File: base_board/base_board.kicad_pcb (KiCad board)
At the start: 2 copper layers, 18 parts, among them J1 Conn_ARM_JTAG_SWD_20, U1 STM32F446ZEJx, U2 IS42S16400J-xT, U3 BMI270

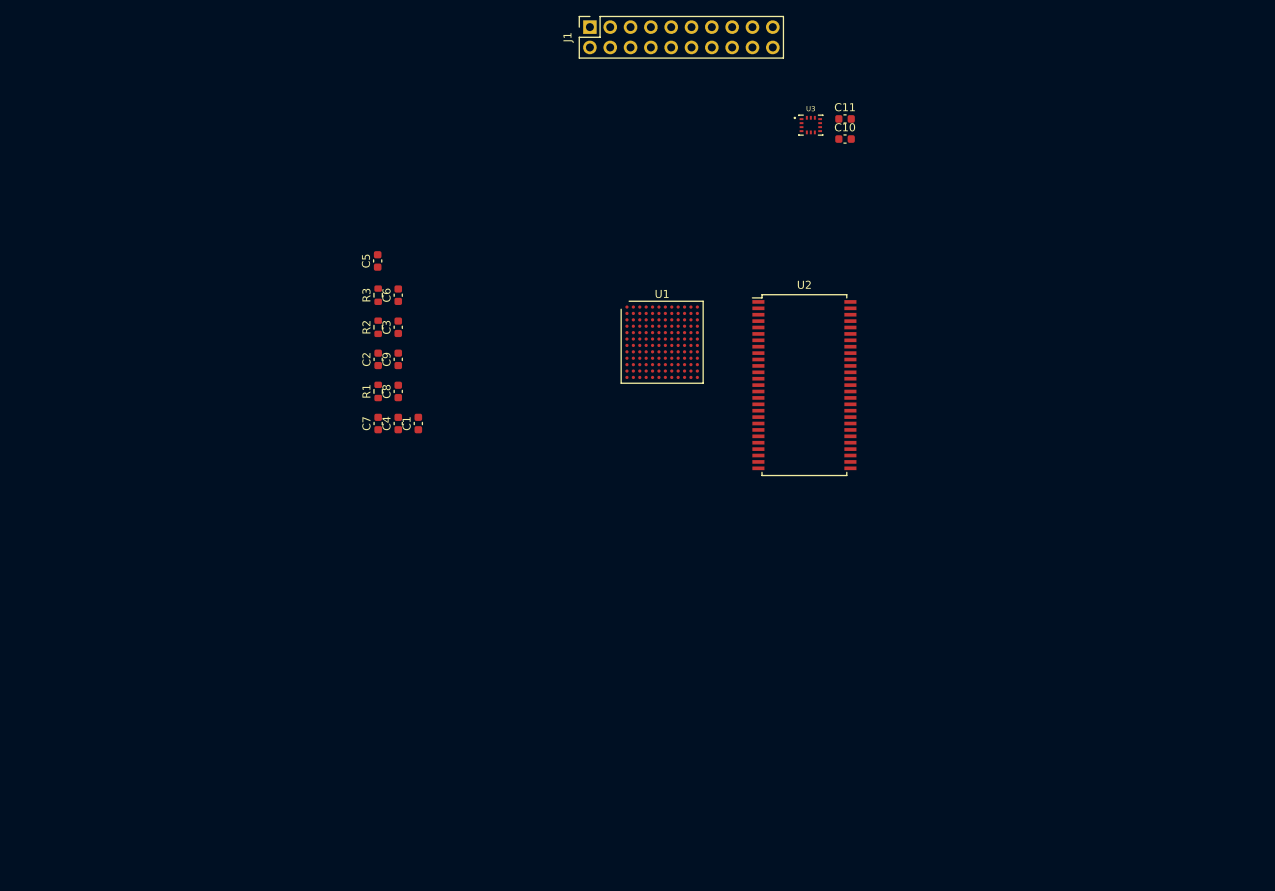
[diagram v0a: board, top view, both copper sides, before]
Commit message: [pcb][cube][schematic] added SWD, Crystal, USB
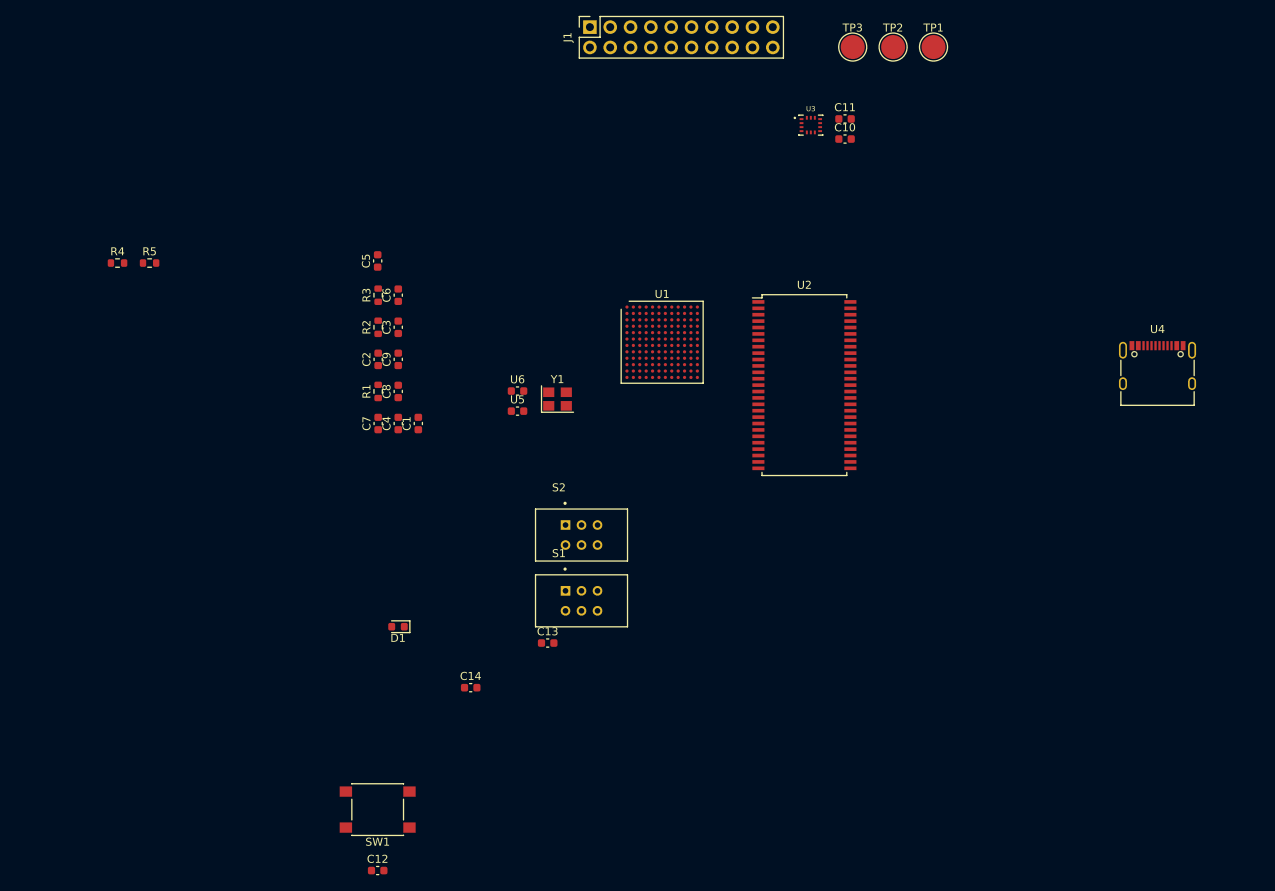
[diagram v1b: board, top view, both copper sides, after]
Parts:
- added C12: 100nF, Capacitor_SMD:C_0603_1608Metric, F.Cu at (96.5, 154.9)
- added C13: 2.2uF, Capacitor_SMD:C_0603_1608Metric, F.Cu at (117.8, 126.5)
- added C14: 2.2uF, Capacitor_SMD:C_0603_1608Metric, F.Cu at (108.2, 132.1)
- added D1: LED, LED_SMD:LED_0603_1608Metric, F.Cu at (99.1, 124.5)
- added R4: 5.1k, Resistor_SMD:R_0603_1608Metric, F.Cu at (64.0, 79.0)
- added R5: 5.1k, Resistor_SMD:R_0603_1608Metric, F.Cu at (68.0, 79.0)
- added S1: EG2209A, project_switch:SW_EG2209A, F.Cu at (122.0, 121.2)
- added S2: EG2209A, project_switch:SW_EG2209A, F.Cu at (122.0, 113.0)
- added SW1: SW_Push, Button_Switch_SMD:SW_Push_1P1T_NO_6x6mm_H9.5mm, F.Cu at (96.5, 147.3)
- added TP1: TestPoint, TestPoint:TestPoint_Pad_D3.0mm, F.Cu at (166.0, 52.0)
- added TP2: TestPoint, TestPoint:TestPoint_Pad_D3.0mm, F.Cu at (160.9, 52.0)
- added TP3: TestPoint, TestPoint:TestPoint_Pad_D3.0mm, F.Cu at (155.9, 52.0)
- added U4: USB_C_Receptacle_USB2.0, project_typec:USB_C_Receptacle_XKB_U262-16XN-4BVC11, F.Cu at (194.0, 93.0)
- added U5: 10p, Capacitor_SMD:C_0603_1608Metric, F.Cu at (114.0, 97.5)
- added U6: 10p, Capacitor_SMD:C_0603_1608Metric, F.Cu at (114.0, 95.0)
- added Y1: Crystal_GND24, Crystal:Crystal_SMD_3225-4Pin_3.2x2.5mm, F.Cu at (119.0, 96.0)
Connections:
- U1 pad C11: unconnected-(U1-PadC11) -> +3.3V
- U1 pad D1: unconnected-(U1-PadD1) -> /HSE_IN
- U1 pad D2: unconnected-(U1-PadD2) -> GND
- U1 pad D3: unconnected-(U1-PadD3) -> +3.3V
- U1 pad E1: unconnected-(U1-PadE1) -> /HSE_OUT
- U1 pad E6: unconnected-(U1-PadE6) -> GND
- U1 pad E7: unconnected-(U1-PadE7) -> GND
- U1 pad F1: unconnected-(U1-PadF1) -> /RESET
- U1 pad F10: unconnected-(U1-PadF10) -> +3.3V
- U1 pad F4: unconnected-(U1-PadF4) -> +3.3V
- U1 pad F5: unconnected-(U1-PadF5) -> +3.3V
- U1 pad F6: unconnected-(U1-PadF6) -> +3.3V
- U1 pad F7: unconnected-(U1-PadF7) -> +3.3V
- U1 pad F8: unconnected-(U1-PadF8) -> +3.3V
- U1 pad F9: unconnected-(U1-PadF9) -> +3.3V
- U1 pad G10: unconnected-(U1-PadG10) -> GND
- U1 pad G4: unconnected-(U1-PadG4) -> GND
- U1 pad G5: unconnected-(U1-PadG5) -> +3.3V
- U1 pad G6: unconnected-(U1-PadG6) -> +3.3V
- U1 pad G7: unconnected-(U1-PadG7) -> +3.3V
- U1 pad G8: unconnected-(U1-PadG8) -> GND
- U1 pad G9: unconnected-(U1-PadG9) -> Net-(C14-Pad2)
- U1 pad H6: unconnected-(U1-PadH6) -> GND
- U1 pad H7: unconnected-(U1-PadH7) -> Net-(C13-Pad2)
- U1 pad J1: unconnected-(U1-PadJ1) -> GND
- U1 pad M1: unconnected-(U1-PadM1) -> +3.3V
- U3 pad 1: unconnected-(U3-Pad1) -> Net-(TP1-Pad1)
- U3 pad 13: unconnected-(U3-Pad13) -> Net-(TP3-Pad1)
- U3 pad 14: unconnected-(U3-Pad14) -> Net-(TP2-Pad1)

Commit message: [schematic][pcb] added usb, signal leds, LDO
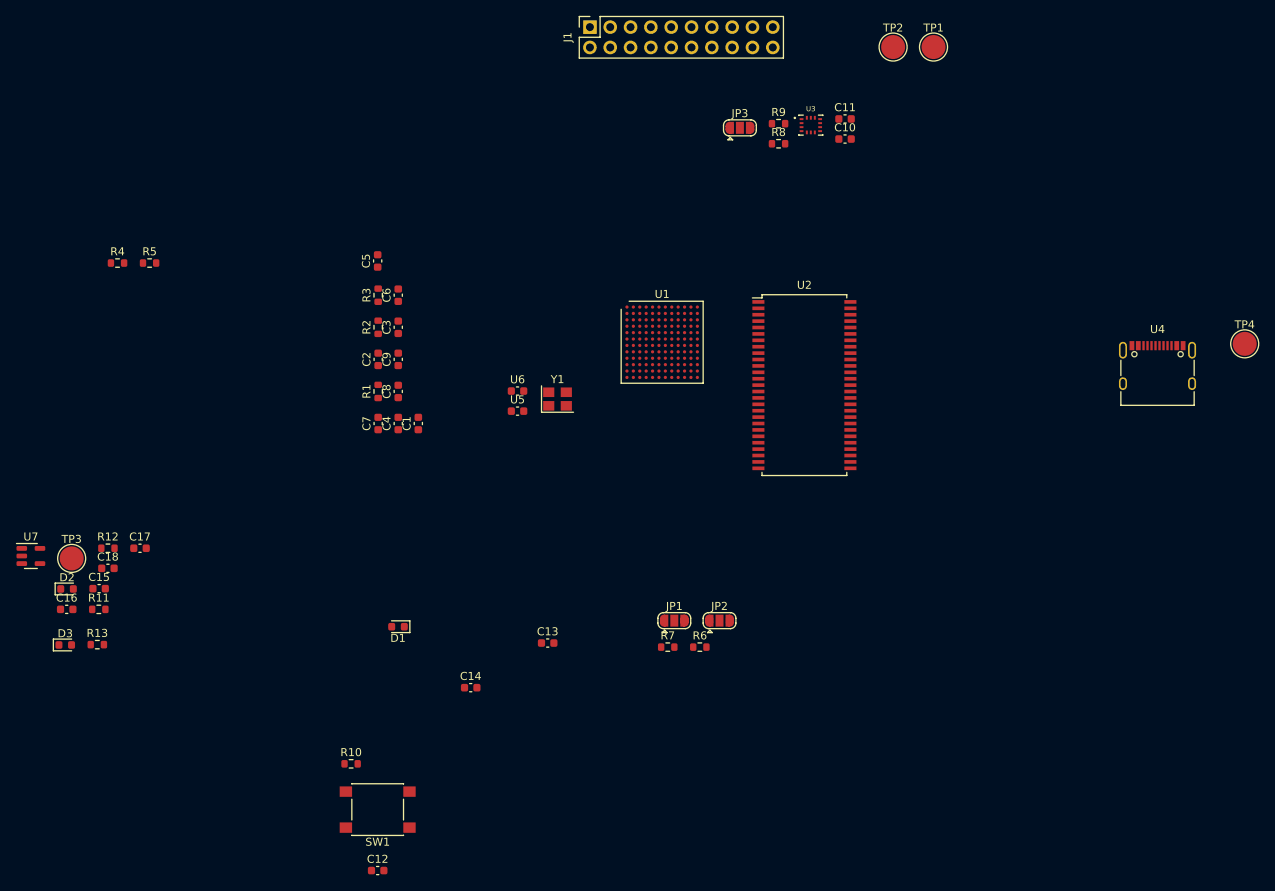
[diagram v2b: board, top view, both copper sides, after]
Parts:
- removed S1, S2: EG2209A, project_switch:SW_EG2209A
- added C15: 1uF, Capacitor_SMD:C_0603_1608Metric, F.Cu at (61.7, 119.7)
- added C16: 100nF, Capacitor_SMD:C_0603_1608Metric, F.Cu at (57.6, 122.3)
- added C17: 10nF, Capacitor_SMD:C_0603_1608Metric, F.Cu at (66.8, 114.7)
- added C18: 1uF, Capacitor_SMD:C_0603_1608Metric, F.Cu at (62.8, 117.2)
- added D2: LED, LED_SMD:LED_0603_1608Metric, F.Cu at (57.7, 119.7)
- added D3: LED, LED_SMD:LED_0603_1608Metric, F.Cu at (57.5, 126.7)
- added JP1: SolderJumper_3_Open, Jumper:SolderJumper-3_P1.3mm_Open_RoundedPad1.0x1.5mm, F.Cu at (133.6, 123.7)
- added JP2: SolderJumper_3_Open, Jumper:SolderJumper-3_P1.3mm_Open_RoundedPad1.0x1.5mm, F.Cu at (139.2, 123.7)
- added JP3: SolderJumper_3_Open, Jumper:SolderJumper-3_P1.3mm_Open_RoundedPad1.0x1.5mm, F.Cu at (141.8, 62.1)
- added R10: 10K, Resistor_SMD:R_0603_1608Metric, F.Cu at (93.2, 141.6)
- added R11: 510, Resistor_SMD:R_0603_1608Metric, F.Cu at (61.7, 122.3)
- added R12: 510, Resistor_SMD:R_0603_1608Metric, F.Cu at (62.8, 114.7)
- added R13: 510, Resistor_SMD:R_0603_1608Metric, F.Cu at (61.5, 126.7)
- added R6: 10K, Resistor_SMD:R_0603_1608Metric, F.Cu at (136.8, 127.0)
- added R7: 10K, Resistor_SMD:R_0603_1608Metric, F.Cu at (132.8, 127.0)
- added R8: 4.7K, Resistor_SMD:R_0603_1608Metric, F.Cu at (146.6, 64.1)
- added R9: 4.7K, Resistor_SMD:R_0603_1608Metric, F.Cu at (146.6, 61.6)
- added TP4: TestPoint, TestPoint:TestPoint_Pad_D3.0mm, F.Cu at (204.9, 89.1)
- added U7: LD3985M33R_SOT23, Package_TO_SOT_SMD:SOT-23-5, F.Cu at (53.2, 115.6)
- moved TP3 116.7 mm to (58.3, 115.9)
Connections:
- D1 pad 1: unconnected-(D1-Pad1) -> GND
- D1 pad 2: unconnected-(D1-Pad2) -> Net-(D1-Pad2)
- TP1 pad 1: Net-(TP1-Pad1) -> /BMI270_SDA
- TP2 pad 1: Net-(TP2-Pad1) -> /BMI270_SCL
- TP3 pad 1: Net-(TP3-Pad1) -> +3V3
- U1 pad B12: unconnected-(U1-PadB12) -> /USB_D+
- U1 pad C12: unconnected-(U1-PadC12) -> /USB_D-
- U1 pad D11: unconnected-(U1-PadD11) -> /USART1_RX
- U1 pad D12: unconnected-(U1-PadD12) -> /USART1_TX
- U1 pad D5: unconnected-(U1-PadD5) -> /BOOT0
- U1 pad J5: unconnected-(U1-PadJ5) -> /BOOT1
- U1 pad L12: unconnected-(U1-PadL12) -> /HEARTBEAT_LED
- U1 pad M11: unconnected-(U1-PadM11) -> /BMI270_INT1
- U1 pad M12: unconnected-(U1-PadM12) -> /BMI270_INT2
- U3 pad 1: Net-(TP1-Pad1) -> Net-(U3-Pad1)
- U3 pad 12: unconnected-(U3-Pad12) -> +3V3
- U3 pad 13: Net-(TP3-Pad1) -> /BMI270_SCL
- U3 pad 14: Net-(TP2-Pad1) -> /BMI270_SDA
- U3 pad 4: unconnected-(U3-Pad4) -> /BMI270_INT1
- U3 pad 5: unconnected-(U3-Pad5) -> +3V3
- U3 pad 8: unconnected-(U3-Pad8) -> +3V3
- U3 pad 9: unconnected-(U3-Pad9) -> /BMI270_INT2
- U4 pad A6: Net-(U4-PadA6) -> /USB_D+
- U4 pad A7: Net-(U4-PadA7) -> /USB_D-
- U4 pad B6: Net-(U4-PadA6) -> /USB_D+
- U4 pad B7: Net-(U4-PadA7) -> /USB_D-

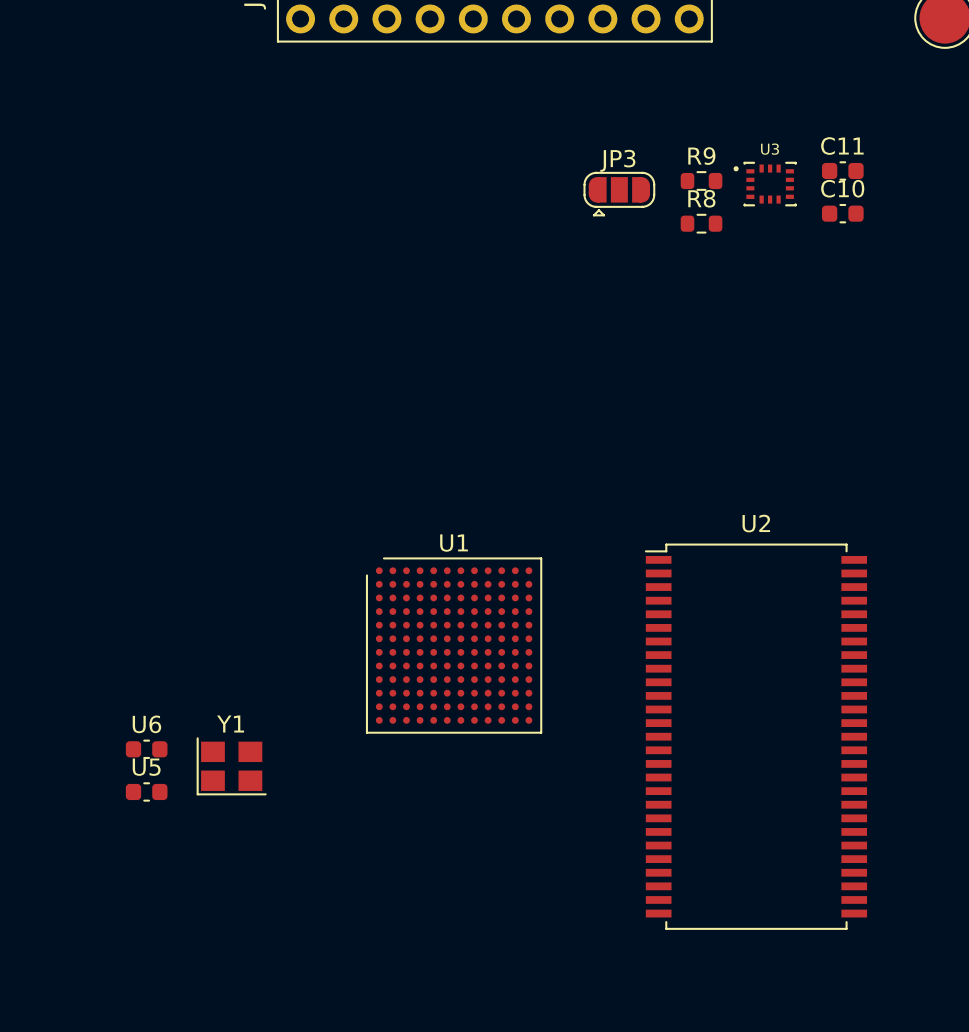
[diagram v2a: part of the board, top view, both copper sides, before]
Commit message: [pcb][schematic] fixed sdram connection. added 6 layers stack
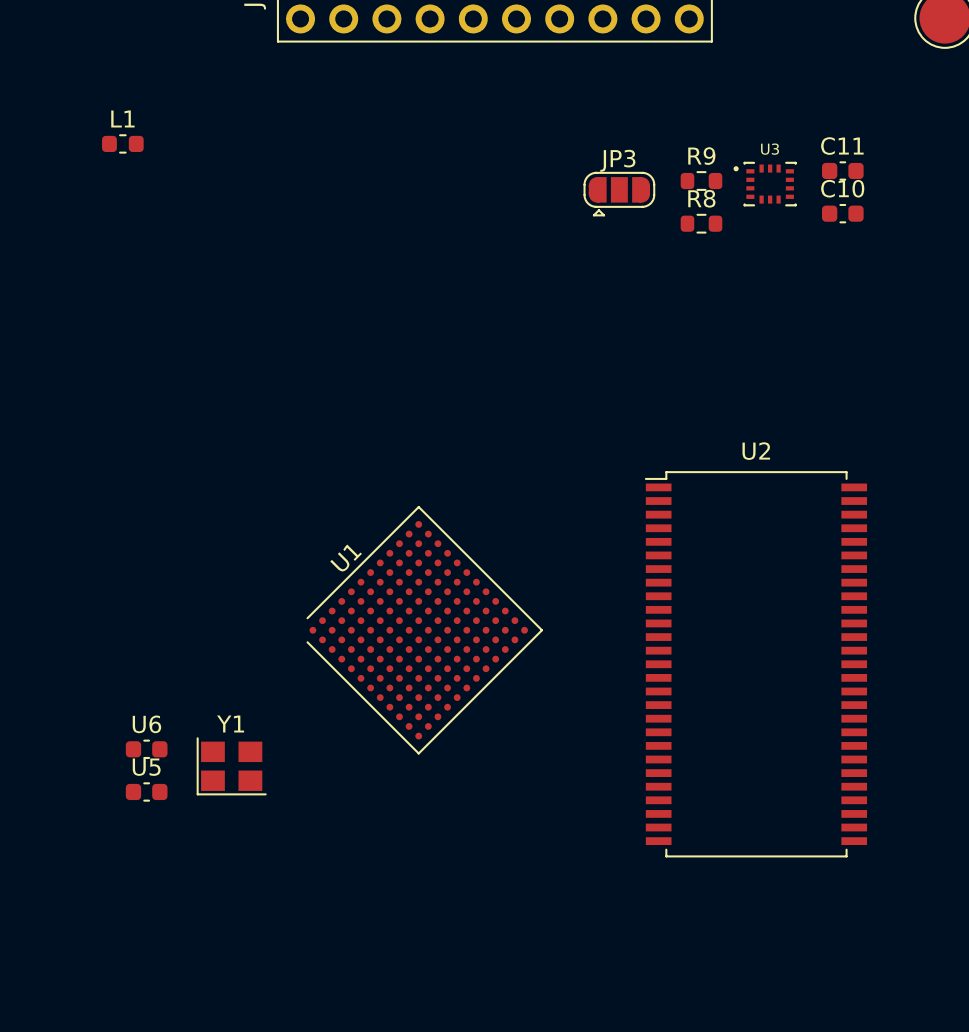
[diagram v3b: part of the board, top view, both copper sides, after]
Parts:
- added L1: INDUCTOR, Inductor_SMD:L_0603_1608Metric, F.Cu at (112.6, 59.4)
- moved U2 4.26 mm to (149.9, 90.0)
- moved U1 2.27 mm to (130.0, 88.0), turned to 45 degrees
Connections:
- U1 pad A1: unconnected-(U1-PadA1) -> /PC13
- U1 pad A2: unconnected-(U1-PadA2) -> /PE3
- U1 pad A3: unconnected-(U1-PadA3) -> /PE2
- U1 pad A8: unconnected-(U1-PadA8) -> /PD6
- U1 pad A9: unconnected-(U1-PadA9) -> /PD7
- U1 pad B1: unconnected-(U1-PadB1) -> /PC14
- U1 pad B10: unconnected-(U1-PadB10) -> /PC11
- U1 pad B11: unconnected-(U1-PadB11) -> /PC10
- U1 pad B2: unconnected-(U1-PadB2) -> /PE4
- U1 pad B3: unconnected-(U1-PadB3) -> /PE5
- U1 pad B4: unconnected-(U1-PadB4) -> /PE6
- U1 pad B9: unconnected-(U1-PadB9) -> /PD5
- U1 pad C1: unconnected-(U1-PadC1) -> /PC15
- U1 pad C10: unconnected-(U1-PadC10) -> /PC12
- U1 pad C11: +3.3V -> Net-(L1-Pad1)
- U1 pad C9: unconnected-(U1-PadC9) -> /PD4
- U1 pad D9: unconnected-(U1-PadD9) -> /PD3
- U1 pad E11: unconnected-(U1-PadE11) -> /PC9
- U1 pad E12: unconnected-(U1-PadE12) -> /PA8
- U1 pad E5: unconnected-(U1-PadE5) -> +3.3V
- U1 pad E9: unconnected-(U1-PadE9) -> /PD2
- U1 pad F11: unconnected-(U1-PadF11) -> /PC8
- U1 pad F12: unconnected-(U1-PadF12) -> /PC7
- U1 pad F2: unconnected-(U1-PadF2) -> /PF7
- U1 pad F3: unconnected-(U1-PadF3) -> /PF6
- U1 pad G1: unconnected-(U1-PadG1) -> /PF10
- U1 pad G12: unconnected-(U1-PadG12) -> /PC6
- U1 pad G2: unconnected-(U1-PadG2) -> /PF9
- U1 pad G3: unconnected-(U1-PadG3) -> /PF8
- U1 pad H2: unconnected-(U1-PadH2) -> /PC1
- U1 pad H3: unconnected-(U1-PadH3) -> /PC2
- U1 pad H4: unconnected-(U1-PadH4) -> /PC3
- U1 pad H9: unconnected-(U1-PadH9) -> /PD11
- U1 pad J2: unconnected-(U1-PadJ2) -> /PA0
- U1 pad J3: unconnected-(U1-PadJ3) -> /PA4
- U1 pad J4: unconnected-(U1-PadJ4) -> /PC4
- U1 pad K10: unconnected-(U1-PadK10) -> /PD13
- U1 pad K2: unconnected-(U1-PadK2) -> /PA1
- U1 pad K3: unconnected-(U1-PadK3) -> /PA5
- U1 pad K4: unconnected-(U1-PadK4) -> /PC5
- U1 pad L10: unconnected-(U1-PadL10) -> /PD12
- U1 pad L2: unconnected-(U1-PadL2) -> /PA2
- U1 pad L3: unconnected-(U1-PadL3) -> /PA6
- U1 pad M1: +3.3V -> Net-(L1-Pad1)
- U1 pad M2: unconnected-(U1-PadM2) -> /PA3
- U1 pad M3: unconnected-(U1-PadM3) -> /PA7
- U2 pad 15: unconnected-(U2-Pad15) -> /FMC_NBL0
- U2 pad 20: /FMC_NBL0 -> /FMC_BA0
- U2 pad 21: /FMC_NBL1 -> /FMC_BA1
- U2 pad 39: unconnected-(U2-Pad39) -> /FMC_NBL1
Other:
- copper layers 2 -> 6
